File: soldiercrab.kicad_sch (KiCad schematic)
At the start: 4 parts, among them J1 MICROMOD-2222, Y1 Osc48MHz

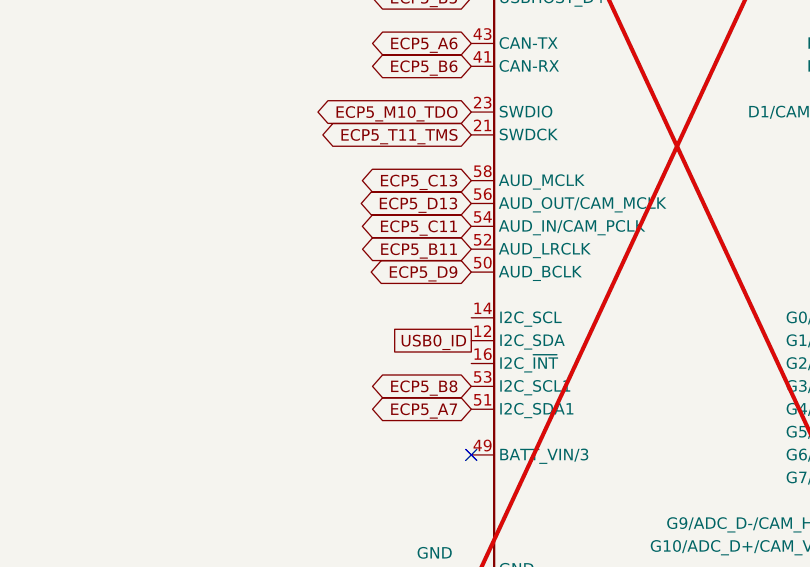
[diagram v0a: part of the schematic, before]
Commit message: Move USB0_ID, connect I2C0_SCL / I2C0_SDA
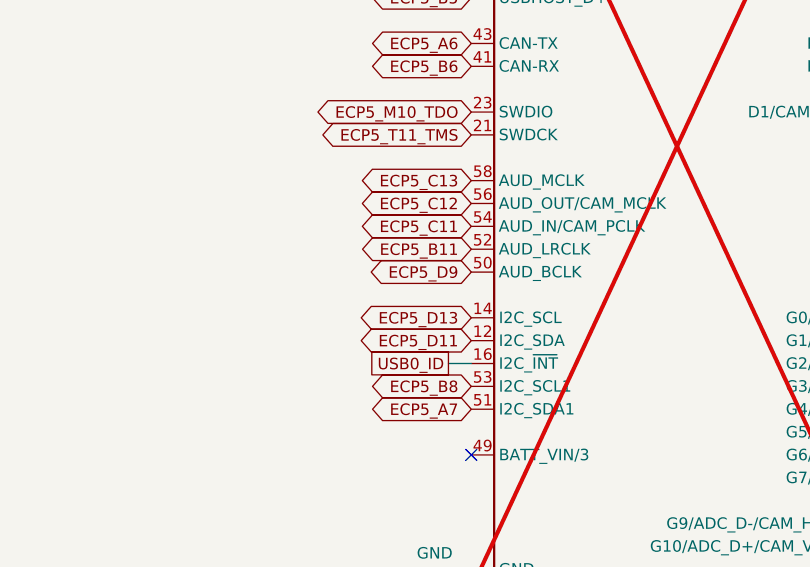
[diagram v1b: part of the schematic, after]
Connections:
- net ECP5_D13: now also J1.14 (I2C_SCL); no longer J1.56 (AUD_OUT/CAM_MCLK)
- net USB0_ID: now also J1.16 (I2C_~{INT}); no longer J1.12 (I2C_SDA)
- new net ECP5_C12: J1.56 (AUD_OUT/CAM_MCLK)
- new net ECP5_D11: J1.12 (I2C_SDA)
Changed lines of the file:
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@@
+	(wire
+		(pts
+			(xy 40.64 110.49) (xy 43.18 110.49)
+		)
+		(stroke
+			(width 0)
+			(type default)
+		)
+	)
 	(wire
 		(pts
@@
 		)
 	)
+	(global_label "ECP5_D11"
+		(shape bidirectional)
+		(at 43.18 107.95 180)
+		(fields_autoplaced yes)
+		(effects
+			(font
+				(size 1.27 1.27)
+			)
+			(justify right)
+		)
+		(property "Intersheetrefs" "${INTERSHEET_REFS}"
+			(at 30.3414 107.95 0)
+			(effects
+				(font
+					(size 1.27 1.27)
+				)
+				(justify right)
+				(hide yes)
+			)
+		)
+	)
 	(global_label "ECP5_B15"
 		(shape bidirectional)
@@
 	(global_label "USB0_ID"
 		(shape passive)
-		(at 43.18 107.95 180)
-		(fields_autoplaced yes)
-		(effects
-			(font
-				(size 1.27 1.27)
-			)
-			(justify right)
-		)
-		(property "Intersheetrefs" "${INTERSHEET_REFS}"
-			(at 33.9396 107.95 0)
+		(at 40.64 110.49 180)
+		(fields_autoplaced yes)
+		(effects
+			(font
+				(size 1.27 1.27)
+			)
+			(justify right)
+		)
+		(property "Intersheetrefs" "${INTERSHEET_REFS}"
+			(at 31.3996 110.49 0)
 			(effects
 				(font
@@
 		(property "Intersheetrefs" "${INTERSHEET_REFS}"
 			(at 31.5509 41.91 0)
+			(effects
+				(font
+					(size 1.27 1.27)
+				)
+				(justify right)
+				(hide yes)
+			)
+		)
+	)
+	(global_label "ECP5_D13"
+		(shape bidirectional)
+		(at 43.18 105.41 180)
+		(fields_autoplaced yes)
+		(effects
+			(font
+				(size 1.27 1.27)
+			)
+			(justify right)
+		)
+		(property "Intersheetrefs" "${INTERSHEET_REFS}"
+			(at 30.3414 105.41 0)
 			(effects
 				(font
@@
 		)
 	)
+	(global_label "ECP5_C12"
+		(shape bidirectional)
+		(at 43.18 92.71 180)
+		(fields_autoplaced yes)
+		(effects
+			(font
+				(size 1.27 1.27)
+			)
+			(justify right)
+		)
+		(property "Intersheetrefs" "${INTERSHEET_REFS}"
+			(at 30.3414 92.71 0)
+			(effects
+				(font
+					(size 1.27 1.27)
+				)
+				(justify right)
+				(hide yes)
+			)
+		)
+	)
 	(global_label "ECP5_C10"
 		(shape bidirectional)
@@
 				(hide yes)
 			)
-		)
-	)
-	(global_label "ECP5_D13"
-		(shape bidirectional)
-		(at 43.18 92.71 180)
-		(fields_autoplaced yes)
-		(effects
-			(font
-				(size 1.27 1.27)
-			)
-			(justify right)
-		)
-		(property "Intersheetrefs" "${INTERSHEET_REFS}"
-			(at 30.3414 92.71 0)
-			(effects
-				(font
-					(size 1.27 1.27)
-				)
-				(justify right)
-				(hide yes)
-			)
